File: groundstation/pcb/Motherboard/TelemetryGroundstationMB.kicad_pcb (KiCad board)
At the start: 2 copper layers, 133 x 79.8 mm, 129 parts, among them J1 USB-C, J10 Conn_01x01, J11 Conn_01x01, J12 USB-C, J2 USB-C, J3 ICD15S13E4GV00LF, J4 USB-C, J5 ICD15S13E4GV00LF, J6 ICD15S13E4GV00LF, J7 ICD15S13E4GV00LF, J8 LD09S33E4GV00LF, J9 Conn_01x04_Socket, M1 M4 Mounting Hole, M2 M4 Mounting Hole, M3 M4 Mounting Hole, M4 M4 Mounting Hole, SW1 SW_Push, SW2 SW_Push, SW3 SW_Push, SW4 SW_Push, SW5 SW_Push, SW6 SW_Push, SW7 SW_Push, SW8 SW_DIP_x01, U1 CP2102N, U2 CP2102N, U3 CP2102N, U5 AVR128DB64x-xPT, U6 MIC29300-3.3WU-TR

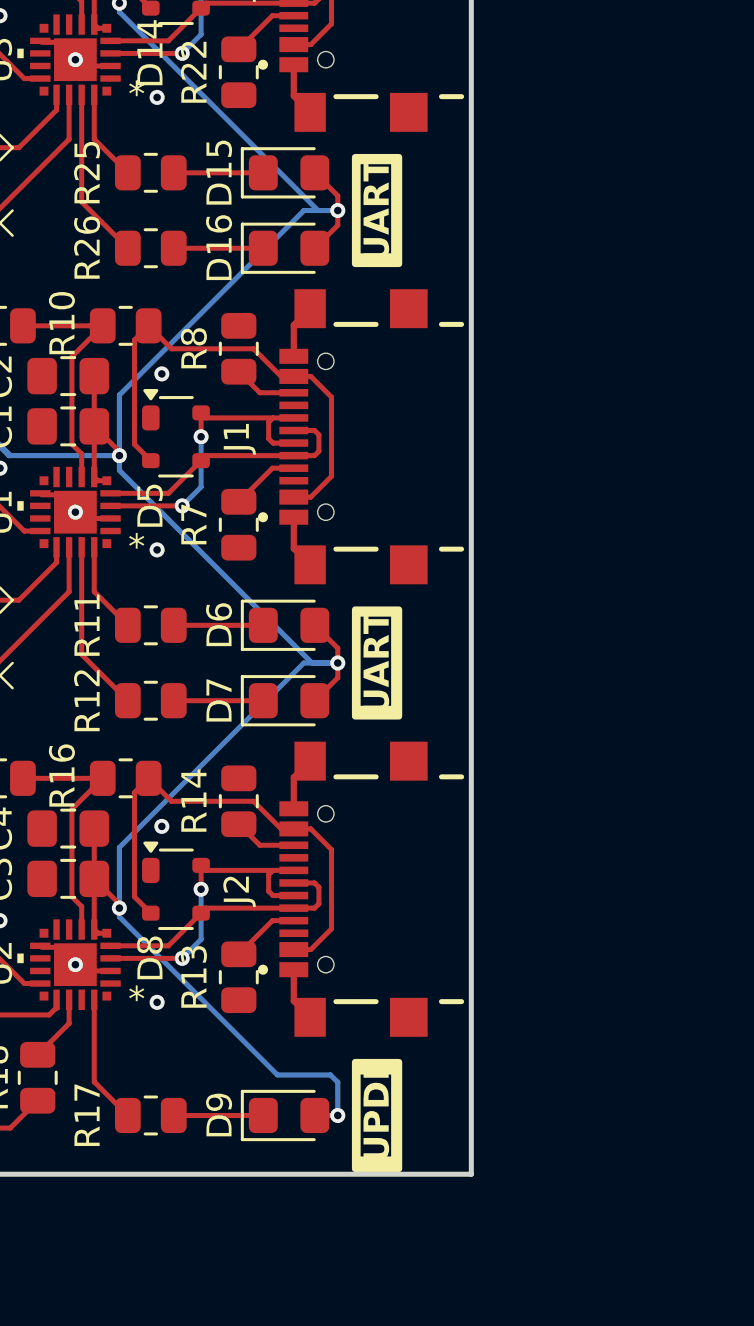
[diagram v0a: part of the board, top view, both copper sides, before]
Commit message: substitute all 3d models
fixes #83
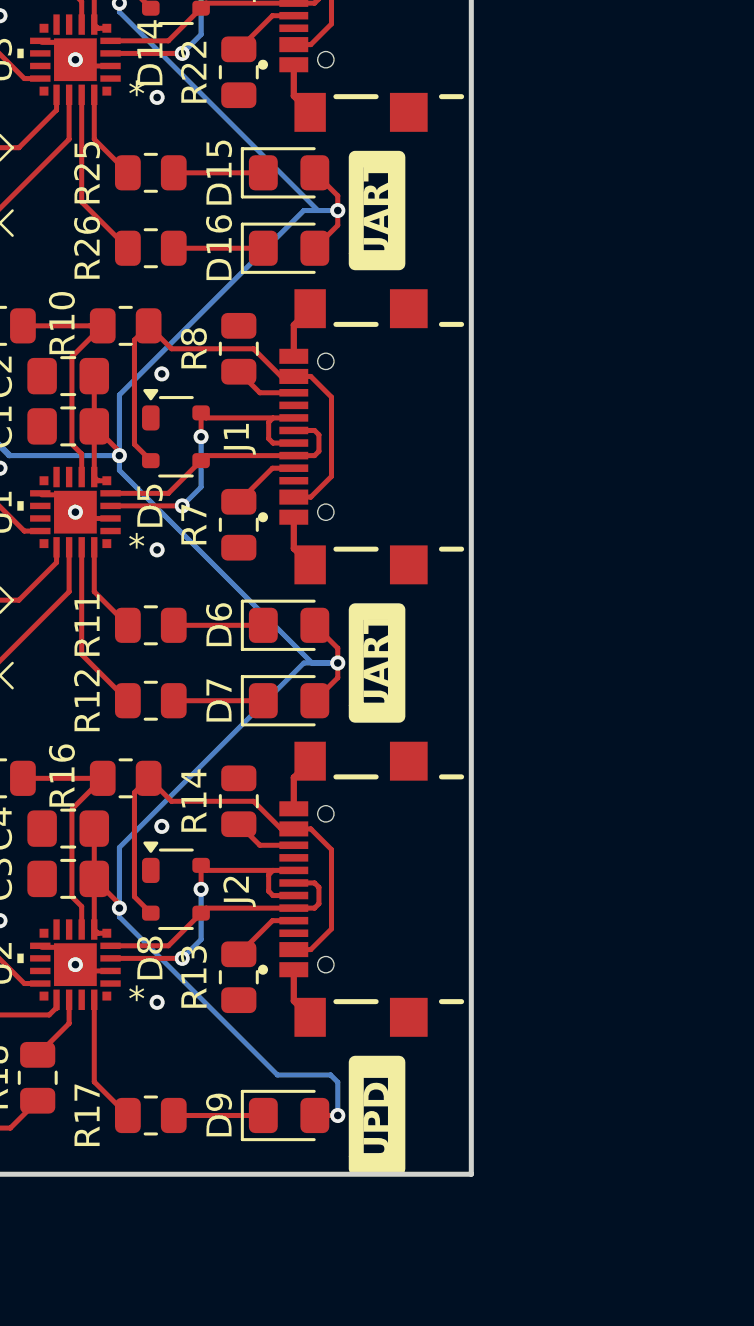
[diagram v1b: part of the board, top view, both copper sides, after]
